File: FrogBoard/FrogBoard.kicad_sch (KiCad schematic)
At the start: 37 parts, among them J1 Conn_01x10, J2 Conn_01x04, J3 USB_B_Micro, J4 Stickbox, J5 Conn_01x03_Socket, J6 Conn_01x02, U1 STM32L432KBUx, U2 USBLC6-2P6, U3 MCP1700T-3302E, U4 BL1555

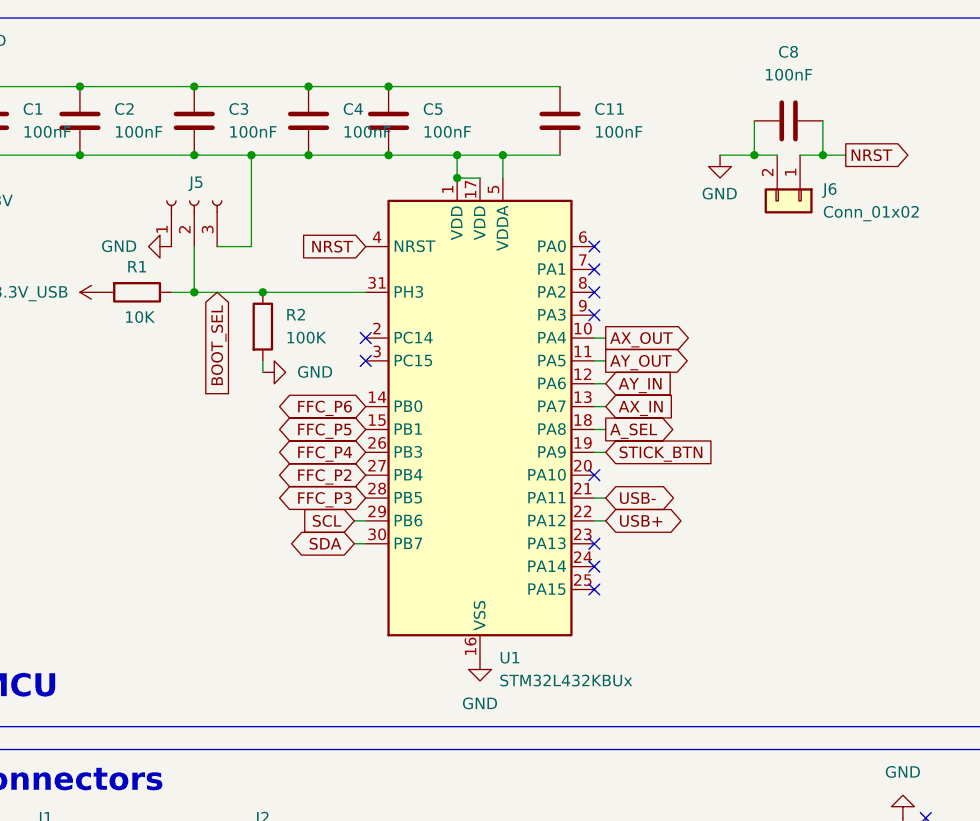
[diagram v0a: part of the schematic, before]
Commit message: Final board layout cleanup, added I2C testpoints
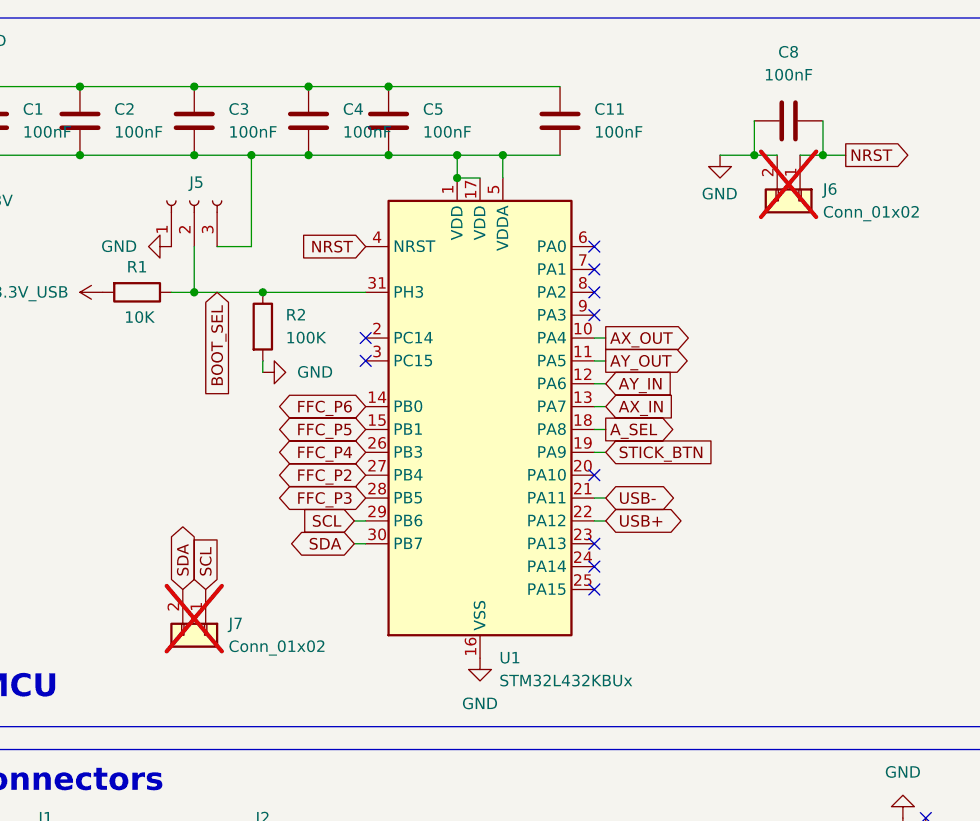
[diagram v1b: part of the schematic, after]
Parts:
- added J7: Conn_01x02, FrogBoard_footprints:PinHeader_1x02_P1.00mm_Vertical_Neutral_No_Coutryard, symbol Connector_Generic:Conn_01x02
- J6: footprint Connector_PinHeader_1.00mm:PinHeader_1x02_P1.00mm_Vertical -> FrogBoard_footprints:PinHeader_1x02_P1.00mm_Vertical_Neutral_No_Coutryard; now not fitted
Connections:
- net SCL: now also J7.1 (Pin_1)
- net SDA: now also J7.2 (Pin_2)
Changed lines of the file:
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@@
 		)
 	)
+	(global_label "SDA"
+		(shape bidirectional)
+		(at 40.64 78.74 90)
+		(fields_autoplaced yes)
+		(effects
+			(font
+				(size 1.27 1.27)
+			)
+			(justify left)
+		)
+		(property "Intersheetrefs" "${INTERSHEET_REFS}"
+			(at 40.64 71.0754 90)
+			(effects
+				(font
+					(size 1.27 1.27)
+				)
+				(justify left)
+				(hide yes)
+			)
+		)
+	)
 	(global_label "BOOT_SEL"
 		(shape input)
@@
 		)
 	)
+	(global_label "SCL"
+		(shape input)
+		(at 43.18 78.74 90)
+		(fields_autoplaced yes)
+		(effects
+			(font
+				(size 1.27 1.27)
+			)
+			(justify left)
+		)
+		(property "Intersheetrefs" "${INTERSHEET_REFS}"
+			(at 43.18 72.2472 90)
+			(effects
+				(font
+					(size 1.27 1.27)
+				)
+				(justify left)
+				(hide yes)
+			)
+		)
+	)
 	(global_label "FFC_P3"
 		(shape bidirectional)
@@
 		(exclude_from_sim no)
 		(in_bom no)
-		(on_board no)
+		(on_board yes)
 		(dnp no)
 		(property "Reference" "J5"
@@
 		(in_bom no)
 		(on_board yes)
-		(dnp no)
+		(dnp yes)
 		(fields_autoplaced yes)
 		(property "Reference" "J6"
@@
 			)
 		)
-		(property "Footprint" "Connector_PinHeader_1.00mm:PinHeader_1x02_P1.00mm_Vertical"
+		(property "Footprint" "FrogBoard_footprints:PinHeader_1x02_P1.00mm_Vertical_Neutral_No_Coutryard"
 			(at 109.22 35.56 0)
 			(effects
@@
 					(unit 1)
 				)
+			)
+		)
+	)
+	(symbol
+		(lib_id "Connector_Generic:Conn_01x02")
+		(at 43.18 83.82 270)
+		(unit 1)
+		(exclude_from_sim yes)
+		(in_bom no)
+		(on_board yes)
+		(dnp yes)
+		(fields_autoplaced yes)
+		(property "Reference" "J7"
+			(at 45.72 82.5499 90)
+			(effects
+				(font
+					(size 1.27 1.27)
+				)
+				(justify left)
+			)
+		)
+		(property "Value" "Conn_01x02"
+			(at 45.72 85.0899 90)
+			(effects
+				(font
+					(size 1.27 1.27)
+				)
+				(justify left)
+			)
+		)
+		(property "Footprint" "FrogBoard_footprints:PinHeader_1x02_P1.00mm_Vertical_Neutral_No_Coutryard"
+			(at 43.18 83.82 0)
+			(effects
+				(font
+					(size 1.27 1.27)
+				)
+				(hide yes)
+			)
+		)
+		(property "Datasheet" "~"
+			(at 43.18 83.82 0)
+			(effects
+				(font
+					(size 1.27 1.27)
+				)
+				(hide yes)
+			)
+		)
+		(property "Description" "Generic connector, single row, 01x02, script generated (kicad-library-utils/schlib/autogen/connector/)"
+			(at 43.18 83.82 0)
+			(effects
+				(font
+					(size 1.27 1.27)
+				)
+				(hide yes)
+			)
+		)
+		(pin "1"
+		)
+		(pin "2"
+		)
+		(instances
+			(project "FrogBoard"
+				(path "/70a1c624-543f-486d-b6f1-90effc8a6c8b"
+					(reference "J7")
+					(unit 1)
+				)

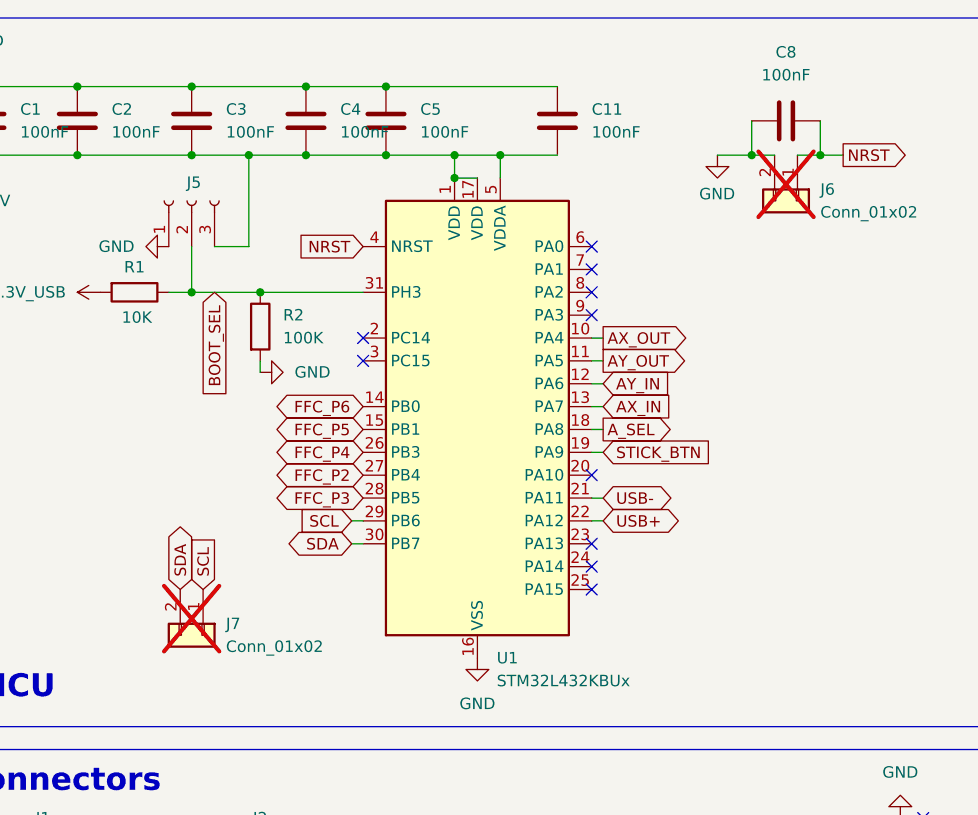
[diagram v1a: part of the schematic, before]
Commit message: Add part numbers, run DRC, add guide
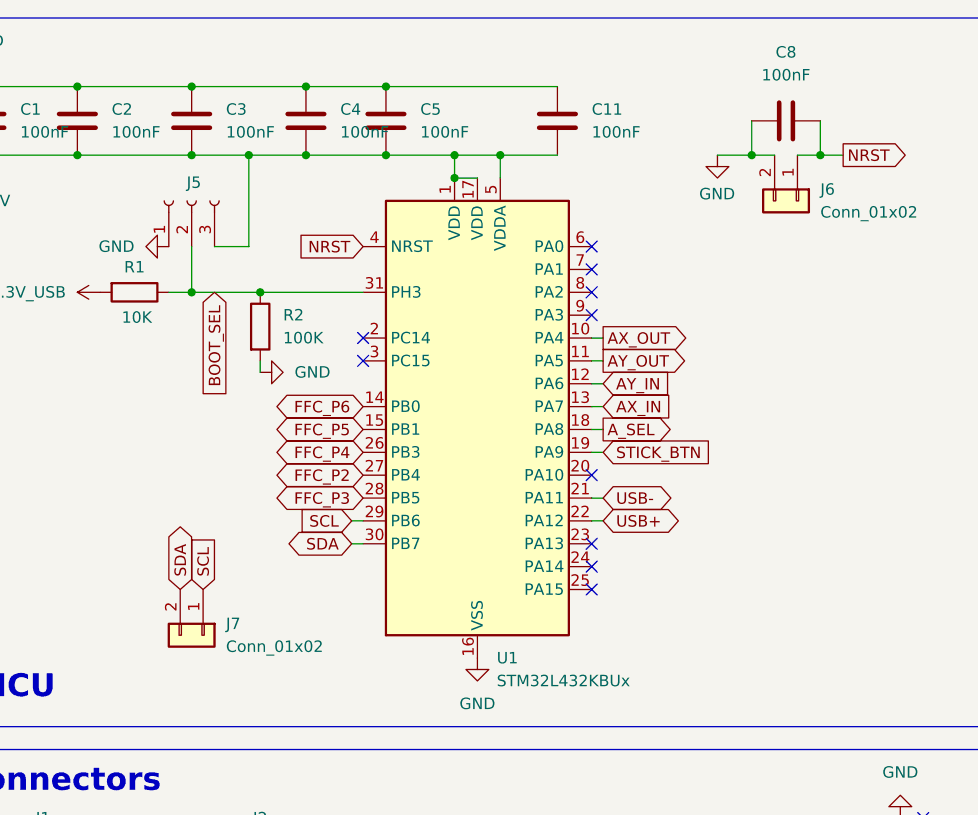
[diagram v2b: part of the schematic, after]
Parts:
- C1, C11, C2, C3, C4, C5, C8: LCSC (none) -> C1591; MPN (none) -> CL10B104KB8NNNC
- J1: LCSC (none) -> C127355; MPN (none) -> 5034801000
- J2: LCSC (none) -> C3170036; MPN (none) -> 528070410
- J3: LCSC (none) -> C132563; MPN (none) -> 10118194-0001LF
- J6, J7: now fitted
- R1: LCSC (none) -> C98220; MPN (none) -> RC0603FR-0710KL
- R2: LCSC (none) -> C14675; MPN (none) -> RC0603FR-07100KL
- R3, R4: LCSC C478866 -> C22548; MPN PTFR0402B1K00P9 -> RC0603FR-071KL
- R5, R6: LCSC C478866 -> C14675; MPN PTFR0402B1K00P9 -> RC0603FR-07100KL
- U1: footprint Package_DFN_QFN:QFN-32-1EP_5x5mm_P0.5mm_EP3.45x3.45mm -> FrogBoard_footprints:QFN-32-1EP_5x5mm_P0.5mm_EP3.45x3.45mm; LCSC (none) -> C2928224; MPN (none) -> STM32L432KBU6TR
- U3: footprint Package_TO_SOT_SMD:SOT-23 -> FrogBoard_footprints:SOT-23
- U4: footprint Package_SO:MSOP-10_3x3mm_P0.5mm -> FrogBoard_footprints:MSOP-10_3x3mm_P0.5mm; LCSC (none) -> C2826598; MPN (none) -> BL1555MM

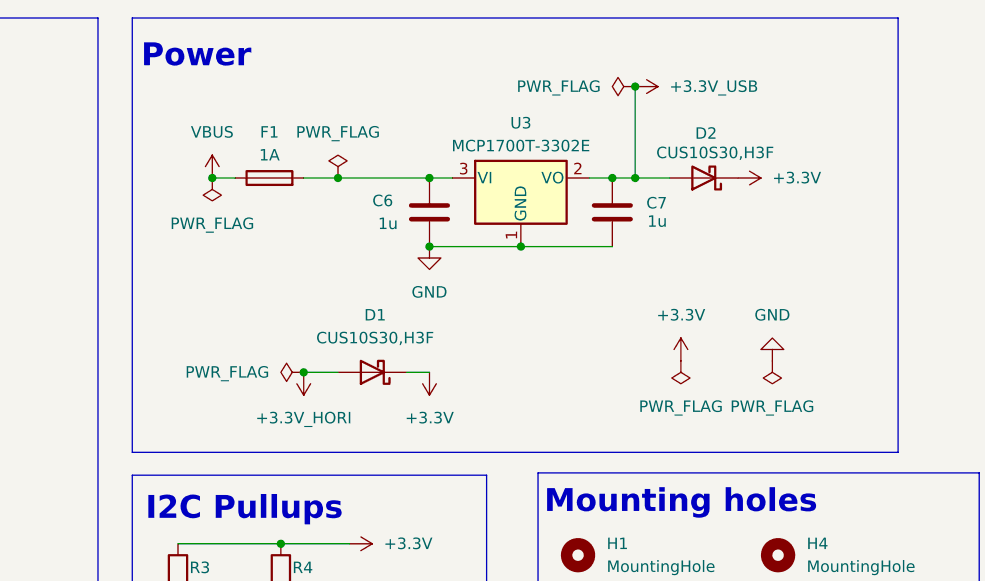
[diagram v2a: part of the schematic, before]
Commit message: Fix ERC/DRC
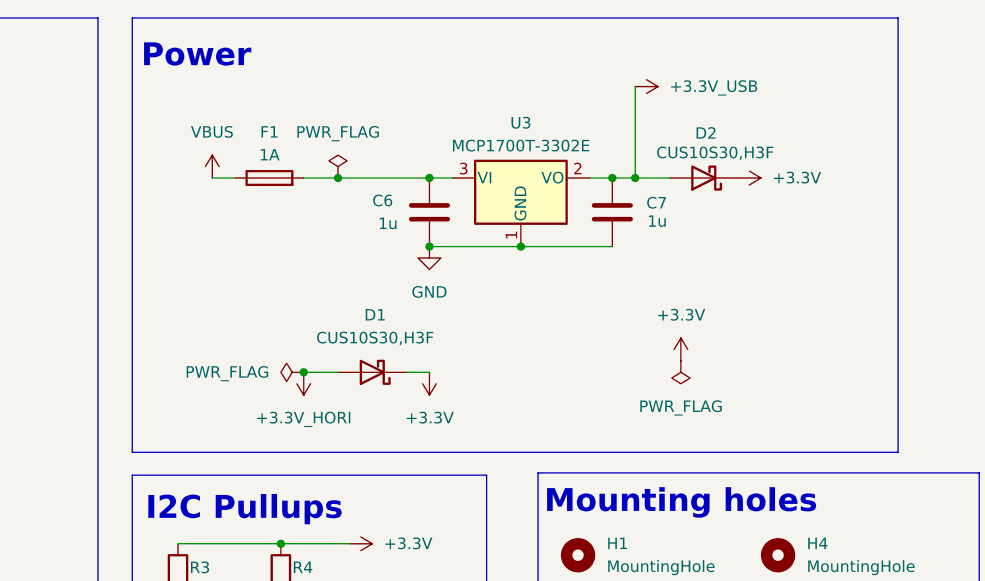
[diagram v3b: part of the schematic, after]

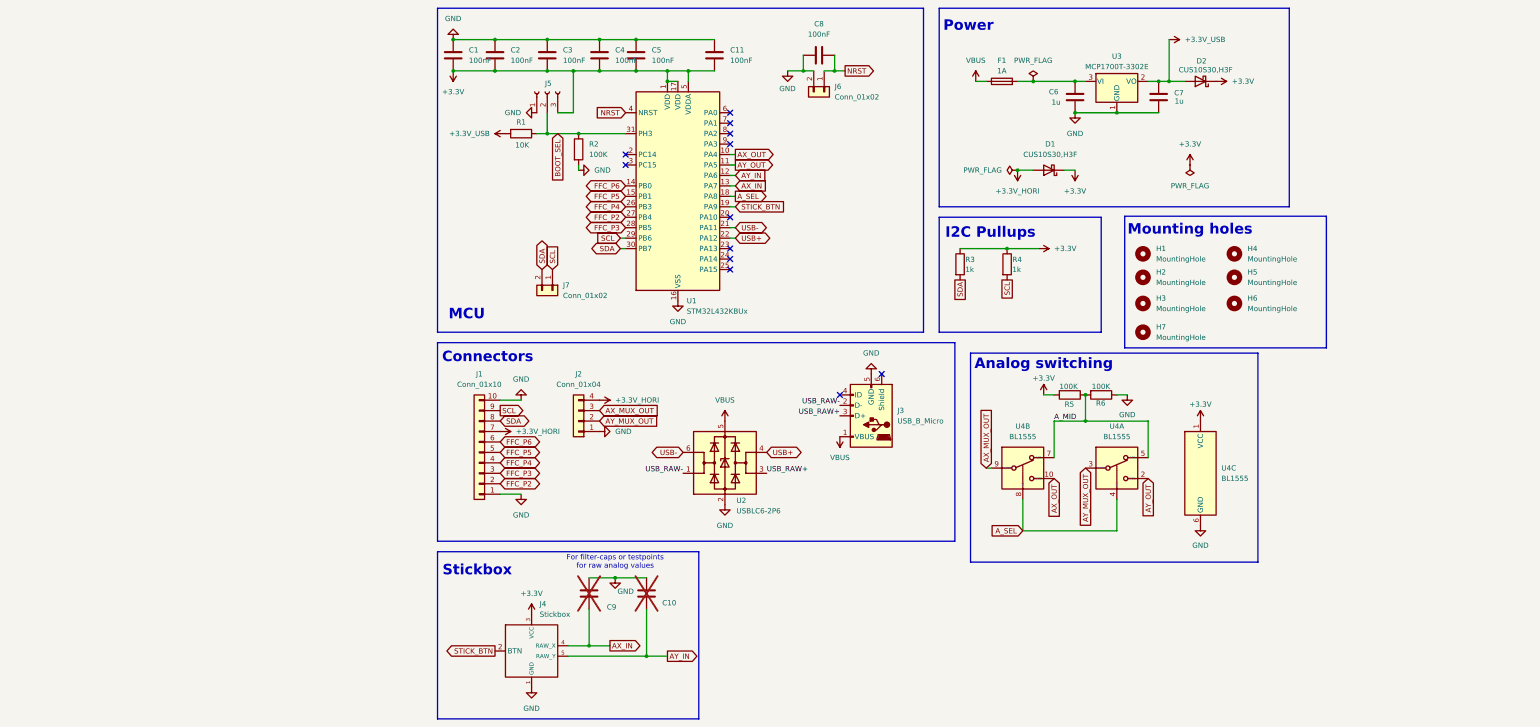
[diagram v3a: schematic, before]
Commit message: removed filter-cap positions and added testpoints for unused MCU pins
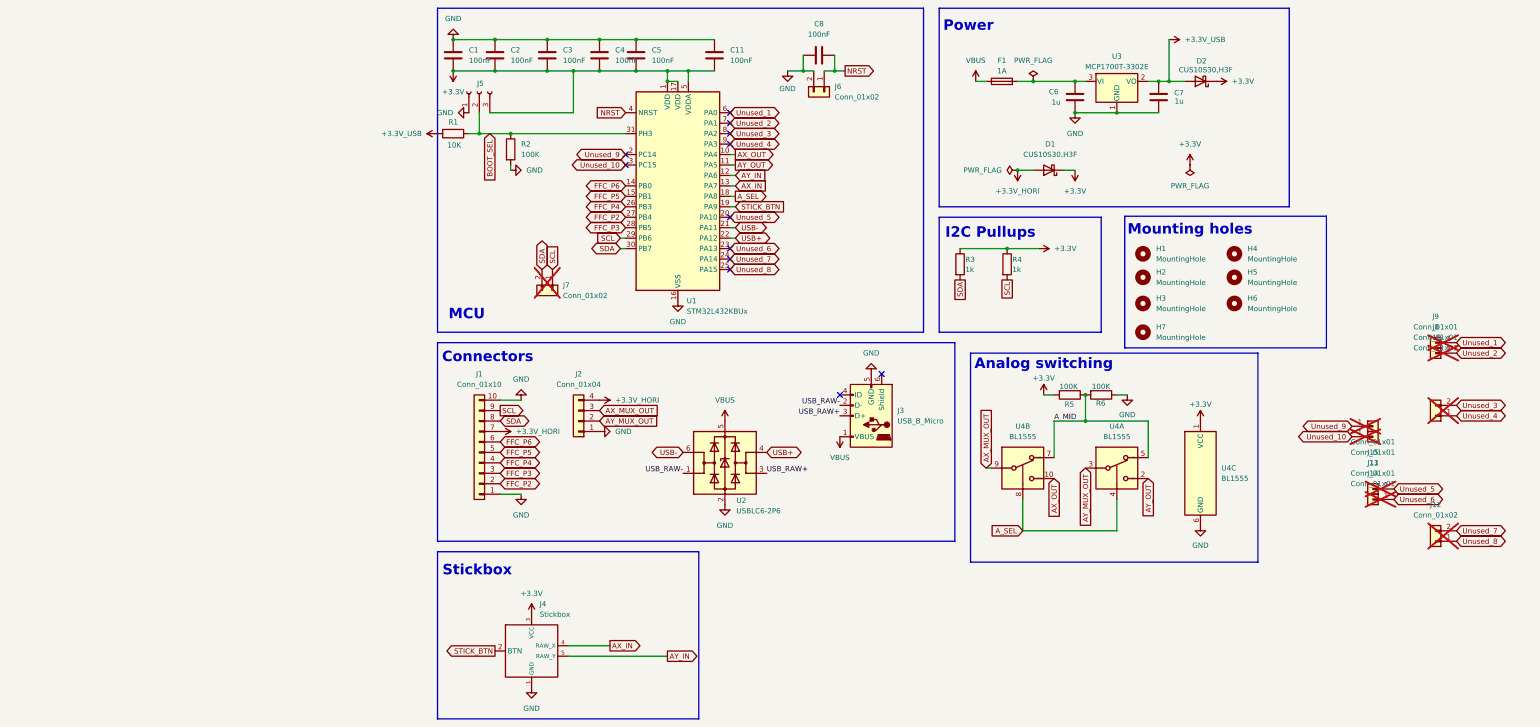
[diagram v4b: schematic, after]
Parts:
- removed C10, C9: ~, Capacitor_THT:C_Disc_D3.0mm_W1.6mm_P2.50mm, symbol Device:C
- added J10, J12: Conn_01x02, FrogBoard_footprints:PinHeader_1x02_P1.00mm_Vertical_Neutral_No_Coutryard, symbol Connector_Generic:Conn_01x02
- added J11, J13, J14, J15, J8, J9: Conn_01x01, FrogBoard_footprints:FrogBoard_PinHeader_1x01_P1.00mm_Vertical, symbol Connector_Generic:Conn_01x01
- J7: now not fitted
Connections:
- net Unused_9: now reaches U1.2 (PC14)
- net Unused_9: now also J15.1 (Pin_1)
- net Unused_5: now reaches U1.20 (PA10)
- net Unused_5: now also J13.1 (Pin_1)
- net Unused_6: now reaches U1.23 (PA13)
- net Unused_6: now also J14.1 (Pin_1)
- net Unused_7: now reaches U1.24 (PA14)
- net Unused_7: now also J12.2 (Pin_2)
- net Unused_8: now reaches U1.25 (PA15)
- net Unused_8: now also J12.1 (Pin_1)
- net Unused_10: now reaches U1.3 (PC15)
- net Unused_10: now also J11.1 (Pin_1)
- net Unused_1: now reaches U1.6 (PA0)
- net Unused_1: now also J9.1 (Pin_1)
- net Unused_2: now reaches U1.7 (PA1)
- net Unused_2: now also J8.1 (Pin_1)
- net Unused_3: now reaches U1.8 (PA2)
- net Unused_3: now also J10.2 (Pin_2)
- net Unused_4: now reaches U1.9 (PA3)
- net Unused_4: now also J10.1 (Pin_1)
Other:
- note removed: "For filter-caps or testpoints for raw analog values"
- moved on the sheet: J5, R1, R2
